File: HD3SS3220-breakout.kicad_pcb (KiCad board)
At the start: 4 copper layers, 7 parts, among them J2 USB_C_Receptacle, U4 HD3SS3220RNHR, U5 U-A-39SS-Y-1, U6 HT7533-1_C14289, U7 TPD4EUSB30, U8 TPD2EUSB30, U9 PZ254-2-08-WS

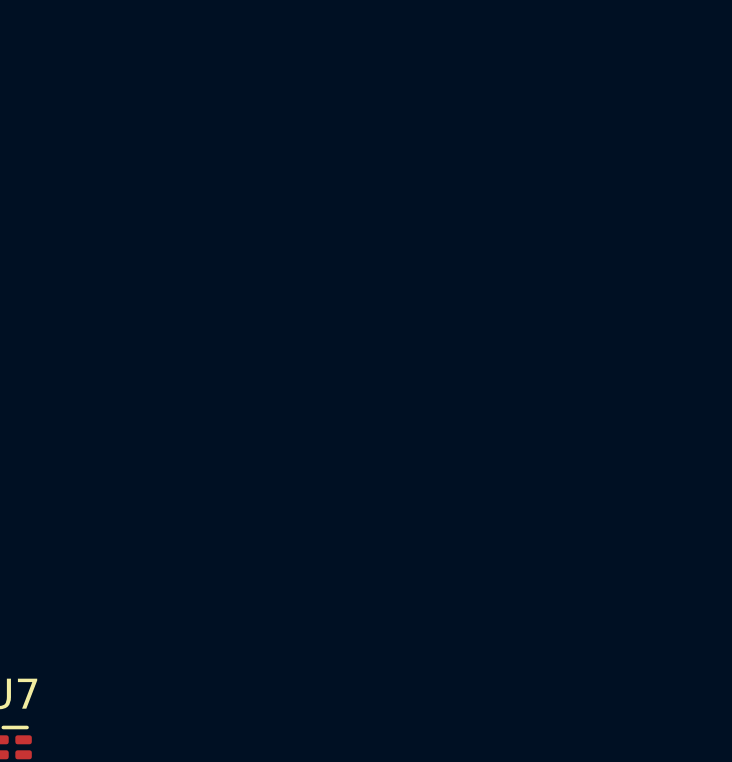
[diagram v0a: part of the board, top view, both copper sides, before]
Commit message: Added dip switch footprint to library and PCB editor
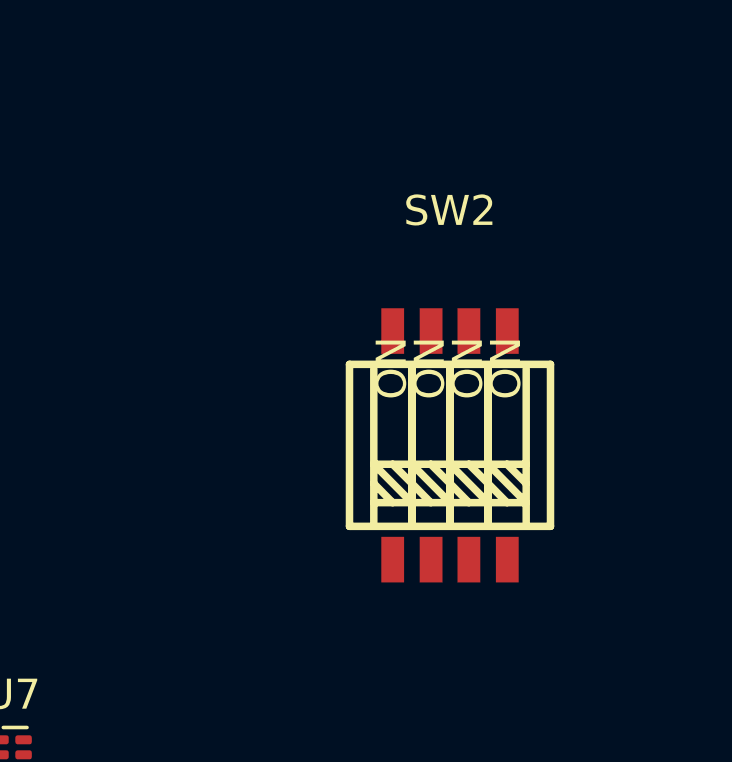
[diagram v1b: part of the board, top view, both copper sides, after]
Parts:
- added SW2: SW_DIP_x04, Button_Switch_SMD:SW4, F.Cu at (179.5, 68.6)

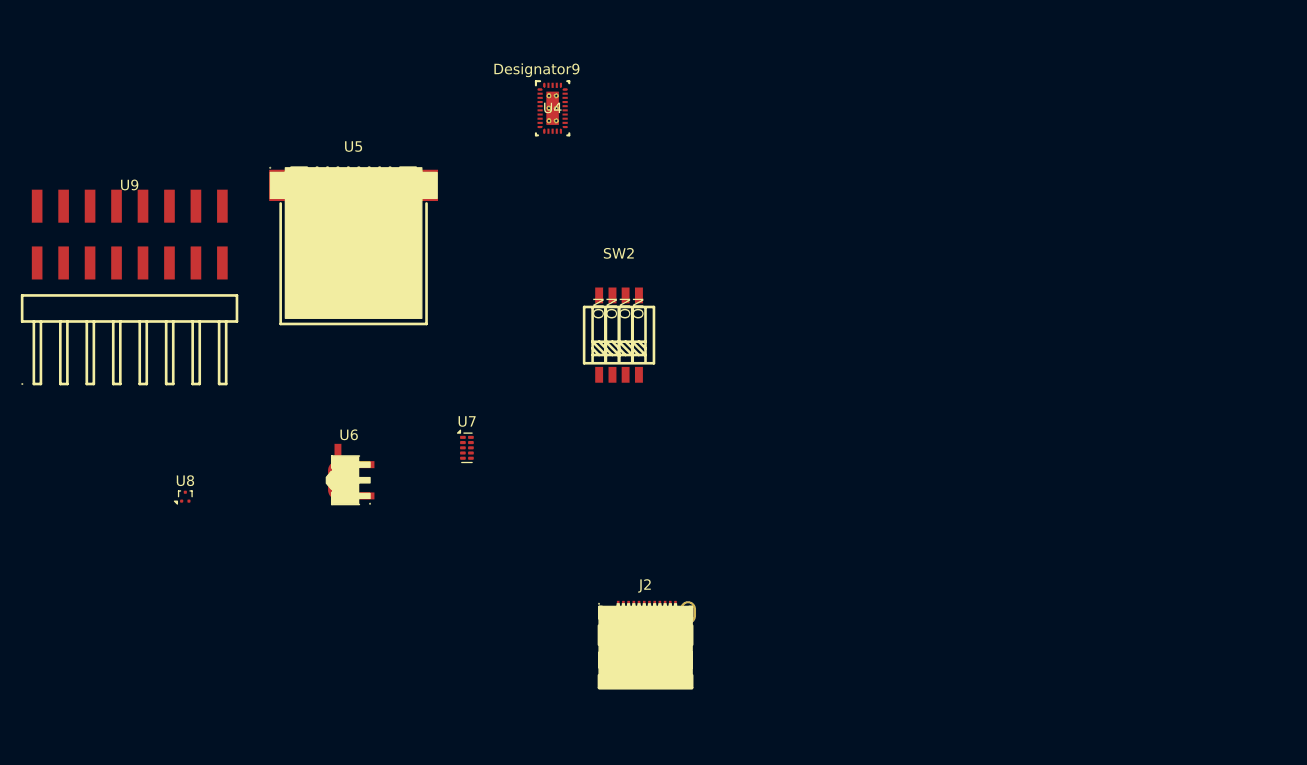
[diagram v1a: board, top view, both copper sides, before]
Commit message: added more footprints
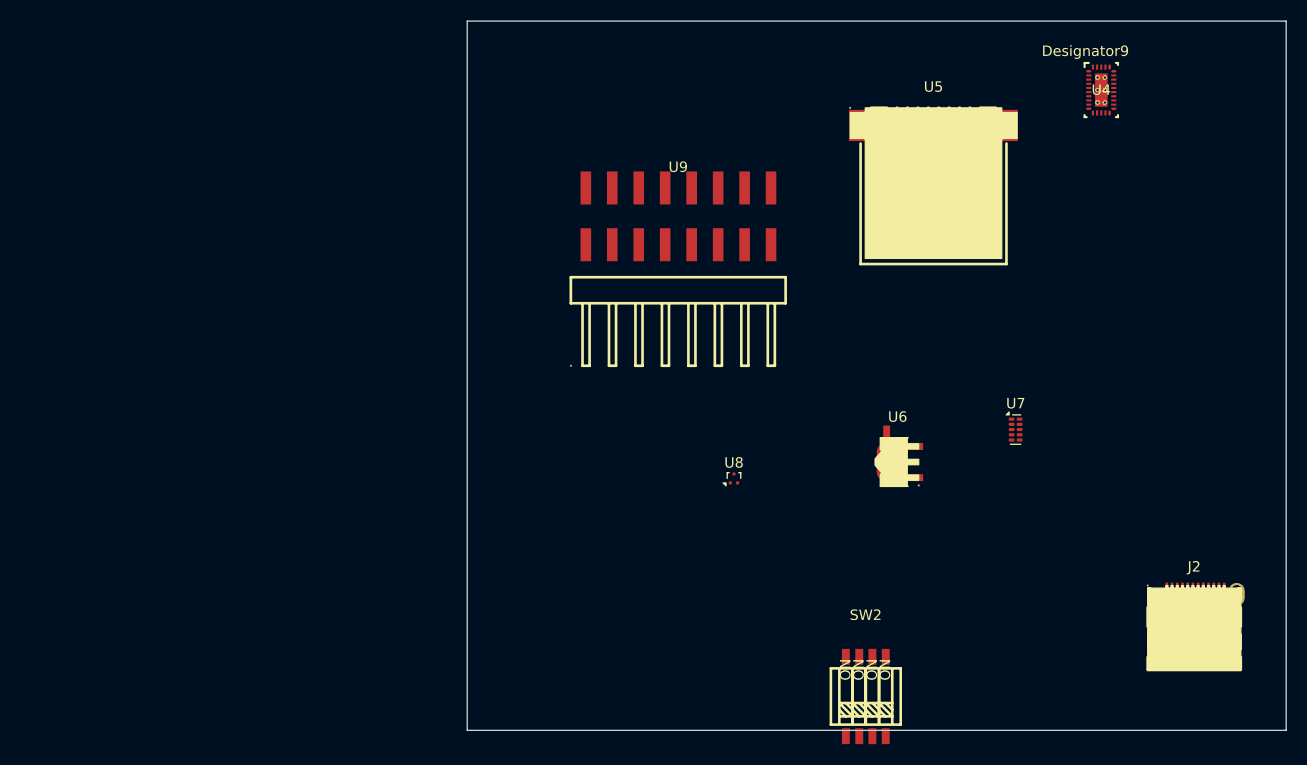
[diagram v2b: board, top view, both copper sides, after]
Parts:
- moved U5 56.0 mm to (209.7, 48.1)
- moved U4 52.7 mm to (225.8, 45.0)
- moved U6 52.7 mm to (206.5, 80.7)
- moved U7 52.7 mm to (217.5, 77.6)
- moved U8 52.7 mm to (190.5, 82.3)
- moved U9 52.7 mm to (185.2, 57.2)
- moved J2 52.7 mm to (234.7, 95.4)
- moved SW2 42.0 mm to (203.2, 103.2)
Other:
- board outline added: 78.6 x 68.1 mm
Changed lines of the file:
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@@
 		(filling no)
 		(pcbplotparams
-			(layerselection 0x00000000_00000000_55555555_5755f5ff)
+			(layerselection 0x00000000_00000000_44dcccc7_7667ddd9)
 			(plot_on_all_layers_selection 0x00000000_00000000_00000000_00000000)
 			(disableapertmacros no)
@@
 	(footprint "footprint:SOT-89-3_L4.5-W2.5-P1.50-LS4.2-BR"
 		(layer "F.Cu")
-		(at 153.856236 82.499873)
+		(at 206.511234 80.749816)
 		(descr "SOT-89-3_L4.5-W2.5-P1.50-LS4.2-BR footprint")
 		(tags "SOT-89-3_L4.5-W2.5-P1.50-LS4.2-BR footprint C14289")
@@
 	(footprint "to-be-organized:USB-C-SMD_TYPE-C-USB-19"
 		(layer "F.Cu")
-		(at 182.024987 97.150057)
+		(at 234.679985 95.4)
 		(descr "USB-C-SMD_TYPE-C-USB-19 footprint")
 		(tags "USB-C-SMD_TYPE-C-USB-19 footprint C106817")
@@
 	(footprint "footprint:HDR-SMD_16P-P2.54-H-M-R2-C8-W12.0-N"
 		(layer "F.Cu")
-		(at 132.519749 58.921812)
+		(at 185.174747 57.171755)
 		(descr "HDR-SMD_16P-P2.54-H-M-R2-C8-W12.0-N footprint")
 		(tags "HDR-SMD_16P-P2.54-H-M-R2-C8-W12.0-N footprint C5149358")
@@
 	(footprint "Package_TO_SOT_SMD:Texas_DRT-3"
 		(layer "F.Cu")
-		(at 137.85 84.075)
+		(at 190.504998 82.324943)
 		(descr "Texas Instrument DRT-3 1x0.8mm Pitch 0.7mm http://www.ti.com/lit/ds/symlink/tpd2eusb30.pdf")
 		(tags "DRT-3 1x0.8mm Pitch 0.7mm")
@@
 	(footprint "Button_Switch_SMD:SW4"
 		(layer "F.Cu")
-		(at 179.475 68.57)
+		(at 203.154998 103.249943)
 		(property "Reference" "SW2"
 			(at 0 -7.81 0)
@@
 	(footprint "Interface_USB:HD3SS3220IRNHR"
 		(layer "F.Cu")
-		(at 173.099998 46.800002)
+		(at 225.754996 45.049945)
 		(tags "HD3SS3220IRNHR ")
 		(property "Reference" "U4"
@@
 	(footprint "footprint:USB-3.0-A_U-A-39SS-Y-1"
 		(layer "F.Cu")
-		(at 154 53.85)
+		(at 209.654998 48.099943)
 		(descr "USB-3.0-A_U-A-39SS-Y-1 footprint")
 		(tags "USB-3.0-A_U-A-39SS-Y-1 footprint C530639")
@@
 	(footprint "Package_SON:USON-10_2.5x1.0mm_P0.5mm"
 		(layer "F.Cu")
-		(at 164.875927 79.384911)
+		(at 217.530925 77.634854)
 		(descr "USON-10 2.5x1.0mm_ Pitch 0.5mm http://www.ti.com/lit/ds/symlink/tpd4e02b04.pdf")
 		(tags "USON-10 2.5x1.0mm Pitch 0.5mm")
@@
 		)
 	)
+	(gr_rect
+		(start 164.903873 38.433898)
+		(end 243.5 106.5)
+		(stroke
+			(width 0.05)
+			(type default)
+		)
+		(fill no)
+		(layer "Edge.Cuts")
+	)
 	(embedded_fonts no)

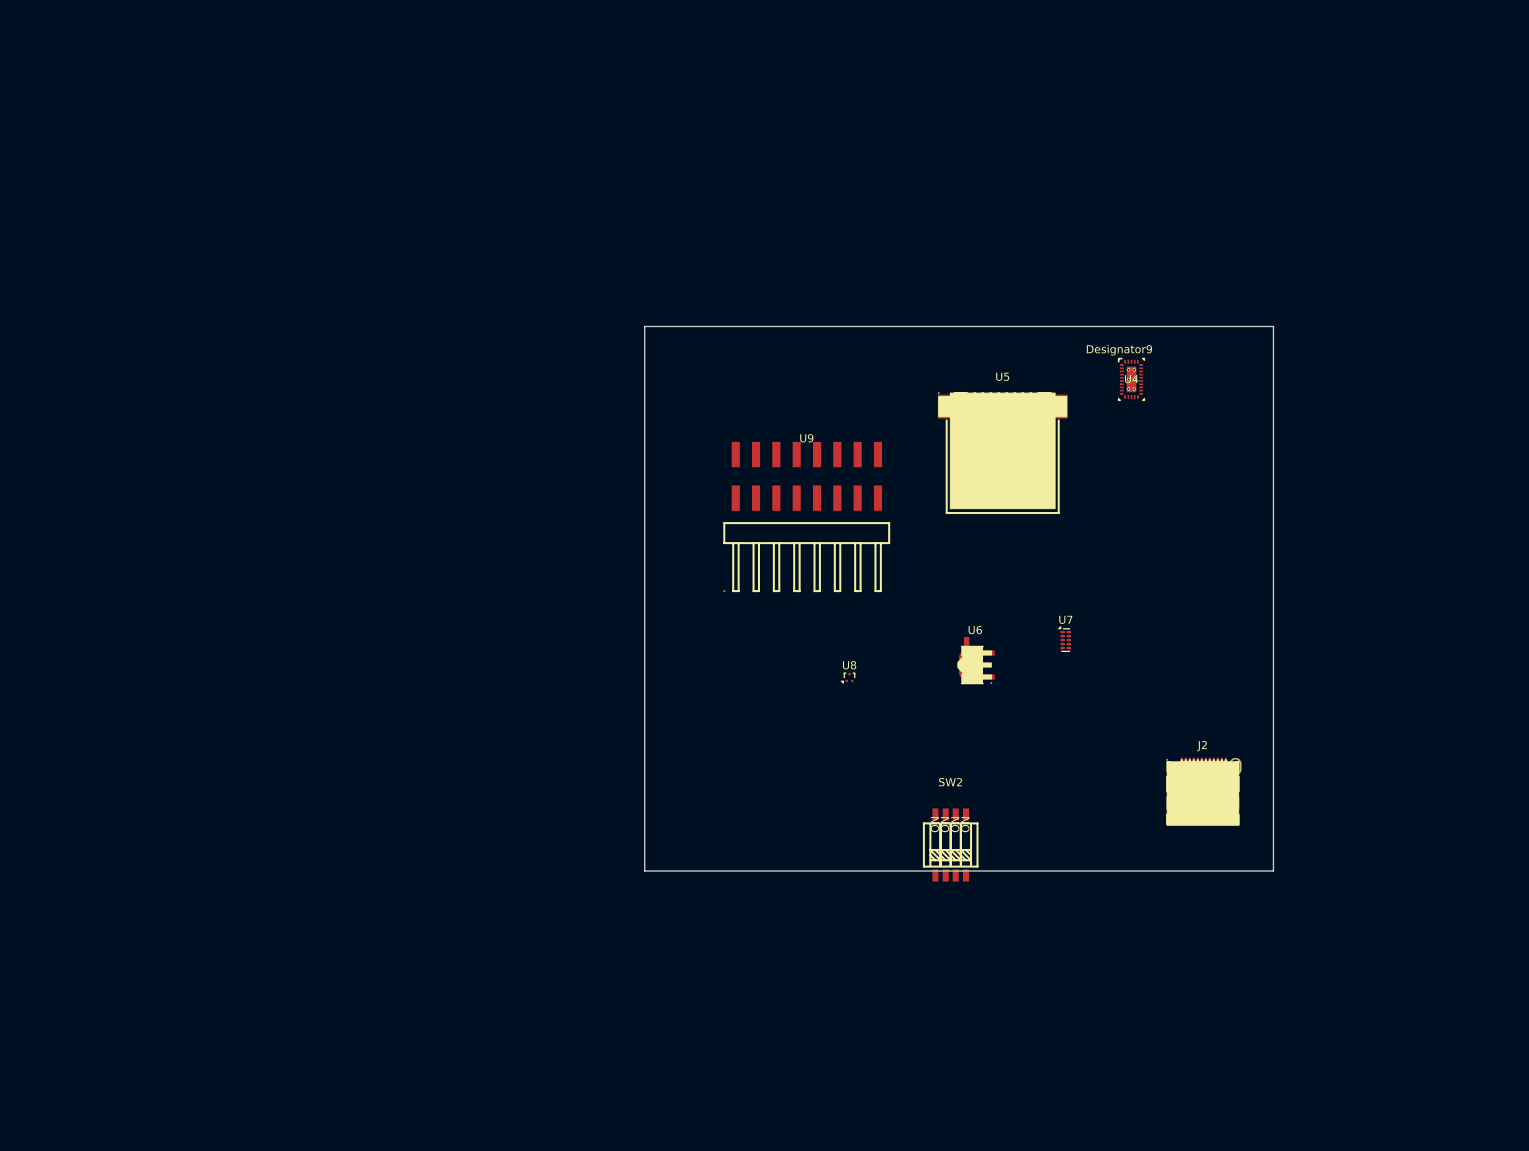
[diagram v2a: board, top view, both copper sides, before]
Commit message: Fixed mux footprint somewhat, starting to route
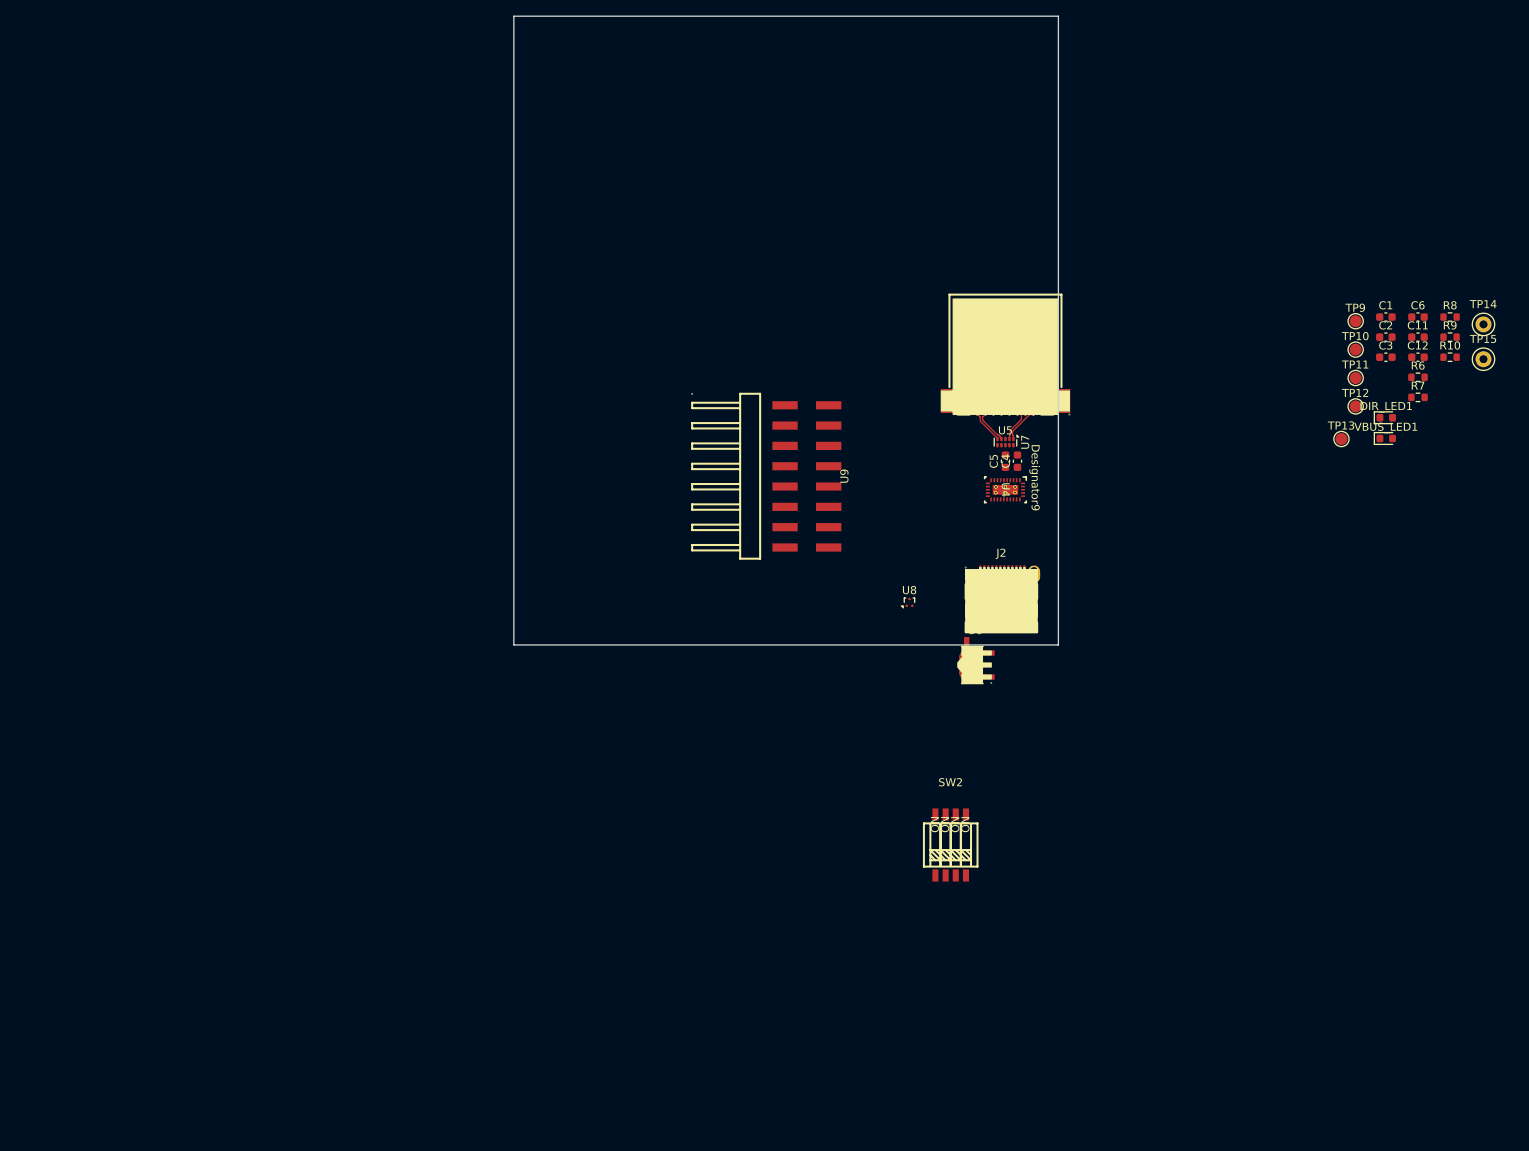
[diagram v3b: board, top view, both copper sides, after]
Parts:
- added C1: 100nF, Capacitor_SMD:C_0603_1608Metric, F.Cu at (257.6, 37.3)
- added C11: 10uF, Capacitor_SMD:C_0603_1608Metric, F.Cu at (261.6, 39.8)
- added C12: 10uF, Capacitor_SMD:C_0603_1608Metric, F.Cu at (261.6, 42.3)
- added C2: 100nF, Capacitor_SMD:C_0603_1608Metric, F.Cu at (257.6, 39.8)
- added C3: 100nF, Capacitor_SMD:C_0603_1608Metric, F.Cu at (257.6, 42.3)
- added C4: 100nF, Capacitor_SMD:C_0603_1608Metric, F.Cu at (211.5, 55.3)
- added C5: 100nF, Capacitor_SMD:C_0603_1608Metric, F.Cu at (210.0, 55.3)
- added C6: 100nF, Capacitor_SMD:C_0603_1608Metric, F.Cu at (261.6, 37.3)
- added DIR_LED1: LED, LED_SMD:LED_0603_1608Metric, F.Cu at (257.6, 49.8)
- added R10: 200K, Resistor_SMD:R_0603_1608Metric, F.Cu at (265.6, 42.3)
- added R6: 1K, Resistor_SMD:R_0603_1608Metric, F.Cu at (261.6, 44.8)
- added R7: 500K, Resistor_SMD:R_0603_1608Metric, F.Cu at (261.6, 47.3)
- added R8: 10K, Resistor_SMD:R_0603_1608Metric, F.Cu at (265.6, 37.3)
- added R9: 900K, Resistor_SMD:R_0603_1608Metric, F.Cu at (265.6, 39.8)
- added TP10: CC2, TestPoint:TestPoint_Pad_D1.5mm, F.Cu at (253.8, 41.3)
- added TP11: VBUS, TestPoint:TestPoint_Pad_D1.5mm, F.Cu at (253.8, 44.9)
- added TP12: VCC33, TestPoint:TestPoint_Pad_D1.5mm, F.Cu at (253.8, 48.4)
- added TP13: VCONN, TestPoint:TestPoint_Pad_D1.5mm, F.Cu at (252.0, 52.5)
- added TP14: GND1, TestPoint:TestPoint_Keystone_5000-5004_Miniature, F.Cu at (269.8, 38.2)
- added TP15: GND2, TestPoint:TestPoint_Keystone_5000-5004_Miniature, F.Cu at (269.8, 42.5)
- added TP9: CC1, TestPoint:TestPoint_Pad_D1.5mm, F.Cu at (253.8, 37.8)
- added VBUS_LED1: LED, LED_SMD:LED_0603_1608Metric, F.Cu at (257.6, 52.4)
- moved J2 34.8 mm to (209.5, 71.4)
- moved U7 25.9 mm to (210.0, 52.9), turned to -90 degrees
- moved U4 20.9 mm to (210.0, 58.8), turned to -90 degrees
- moved U8 12.0 mm to (198.0, 72.9)
- moved U5 0.35 mm to (210.0, 48.1), turned to 180 degrees
- turned U9 to -90 degrees
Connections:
- U4 pad 6: Net-(U4-TXp) -> /SSTXMUX+
- U4 pad 7: Net-(U4-TXn) -> /SSTXMUX-
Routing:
- net /SSTX+: track 0.00 -> 5.71 mm
- net /SSRX+: track 0.00 -> 5.48 mm
- net /SSRX-: track 0.00 -> 5.29 mm
- net /SSTX-: track 0.00 -> 4.67 mm
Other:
- board size 78.6 x 68.1 mm -> 68.1 x 78.6 mm

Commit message: routing
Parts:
- moved C3 81.8 mm to (176.0, 36.5), turned to 180 degrees
- moved C1 77.4 mm to (180.3, 32.5)
- moved C2 77.4 mm to (180.3, 35.0)
- moved C6 76.6 mm to (185.0, 35.5)
- moved U9 57.3 mm to (129.7, 42.9)
- moved U4 43.3 mm to (171.5, 39.0), turned to 0 degrees
- moved J2 41.4 mm to (180.0, 42.4)
- moved VBUS_LED1 11.4 mm to (268.7, 55.0)
- moved DIR_LED1 10.6 mm to (268.2, 50.5)
- moved R7 7.37 mm to (260.0, 54.5)
- moved R6 6.02 mm to (259.7, 50.5)
- moved U6 4.66 mm to (201.9, 81.0)
- moved C5 0.50 mm to (209.5, 55.3)
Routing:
- net /RX1-: track 0.00 -> 8.78 mm
- net /RX1+: track 0.00 -> 8.68 mm

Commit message: cursed vias
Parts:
- moved U9 31.9 mm to (159.5, 31.5)
- moved SW2 30.9 mm to (234.1, 103.2)
- moved U6 30.9 mm to (232.8, 80.9)
- moved C1 29.6 mm to (190.3, 60.3), turned to 90 degrees
- moved J2 28.3 mm to (185.3, 70.2)
- moved C3 27.1 mm to (188.8, 60.3), turned to 90 degrees
- moved U5 25.7 mm to (186.5, 37.8)
- moved U7 25.7 mm to (186.5, 42.6)
- moved C4 25.6 mm to (187.0, 47.7)
- moved C2 25.6 mm to (183.8, 60.3), turned to -90 degrees
- moved C5 25.2 mm to (185.5, 47.7)
- moved C6 25.0 mm to (182.3, 60.3), turned to -90 degrees
- moved U4 20.6 mm to (185.8, 53.8), turned to -90 degrees
- moved U8 11.4 mm to (193.5, 62.5)
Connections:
- C1 pad 2: Net-(U4-TX2p) -> /TX2+
- C2 pad 2: Net-(U4-TX1p) -> /TX1+
- C3 pad 2: Net-(U4-TX2n) -> /TX2-
- C6 pad 2: Net-(U4-TX1n) -> /TX1-
- U4 pad 16: Net-(U4-TX1n) -> /TX1-
- U4 pad 17: Net-(U4-TX1p) -> /TX1+
- U4 pad 20: Net-(U4-TX2n) -> /TX2-
- U4 pad 21: Net-(U4-TX2p) -> /TX2+
- U7 pad 10: unconnected-(U7-NC-Pad10) -> /SSTX+
- U7 pad 6: unconnected-(U7-NC-Pad6) -> /SSRX-
- U7 pad 7: unconnected-(U7-NC-Pad7) -> /SSRX+
- U7 pad 9: unconnected-(U7-NC-Pad9) -> /SSTX-
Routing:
- net /TX2-: track 0.00 -> 25.0 mm, vias 0 -> 2
- net /TX2+: track 0.00 -> 24.4 mm, vias 0 -> 2
- net /TX1-: track 0.00 -> 16.5 mm, vias 0 -> 2
- net /TX1+: track 0.00 -> 16.5 mm, vias 0 -> 2
- net /RX1-: track 8.78 -> 24.9 mm
- net /RX1+: track 8.68 -> 24.7 mm
- net /RX2-: track 0.00 -> 13.6 mm
- net /RX2+: track 0.00 -> 13.6 mm
- net /SSRX+: track 5.48 -> 15.9 mm
- net /SSRX-: track 5.29 -> 15.6 mm
- net /SSTXMUX+: track 0.00 -> 4.78 mm
- net /SSTX-: track 4.67 -> 9.35 mm
- net /SSTXMUX-: track 0.03 -> 4.27 mm
- net /SSTX+: track 5.71 -> 9.89 mm
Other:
- board size 68.1 x 78.6 mm -> 74.1 x 58 mm
